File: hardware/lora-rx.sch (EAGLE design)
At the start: 31 parts, among them J1 USB-A-H, J2 SMA_EDGE, J3 DNP, U1 STM32L052K8, U2 SX1278, U3 TPS70933

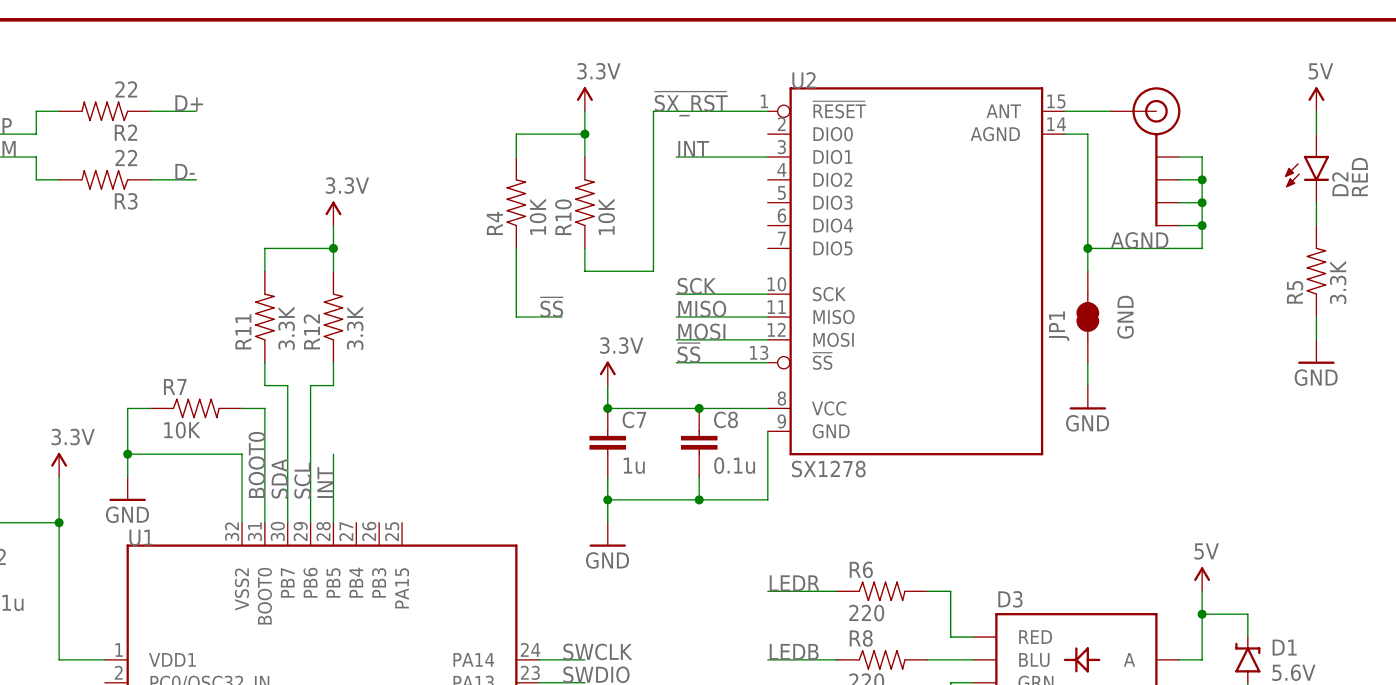
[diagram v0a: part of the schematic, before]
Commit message: Initial route for HAB v3 modular base board
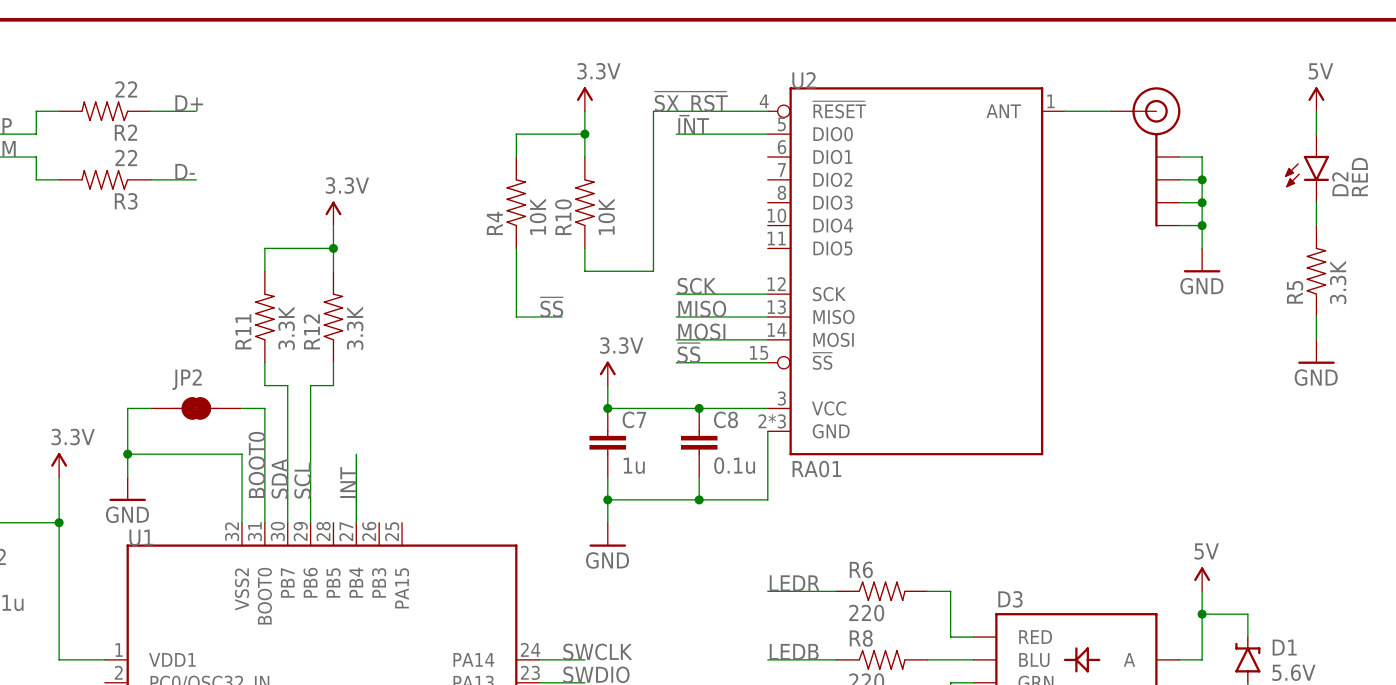
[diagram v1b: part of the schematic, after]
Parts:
- removed JP1: GND, SparkFun-Passives:JUMPER-PAD-2-NC_BY_TRACE
- removed R7: 10K, SparkFun-Passives:RESISTOR0805-RES
- added JP2: JUMPER-SMT_2_NC_TRACE_NO-SILK, SparkFun-Jumpers:JUMPER-SMT_2_NC_TRACE_NO-SILK
- U2: value SX1278 -> RA01; device HAB:DRF1278F -> HAB:RA01
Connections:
- removed net AGND: J2.GND@0, J2.GND@1, J2.GND@2, J2.GND@3, JP1.2, U2.AGND
- net BOOT0: now also JP2.2; no longer R7.2
- net GND: now also J2.GND@0, J2.GND@1, J2.GND@2, J2.GND@3, JP2.1; no longer JP1.1, R7.1
- net INT: now also U1.PB4, U2.DIO0; no longer U1.PB5, U2.DIO1
